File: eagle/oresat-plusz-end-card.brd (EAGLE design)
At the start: 99 x 95.3 mm, 13 parts, among them J1 J-SAMTEC-TFM-110-X1-XXX-D-RA, J2 U.FL

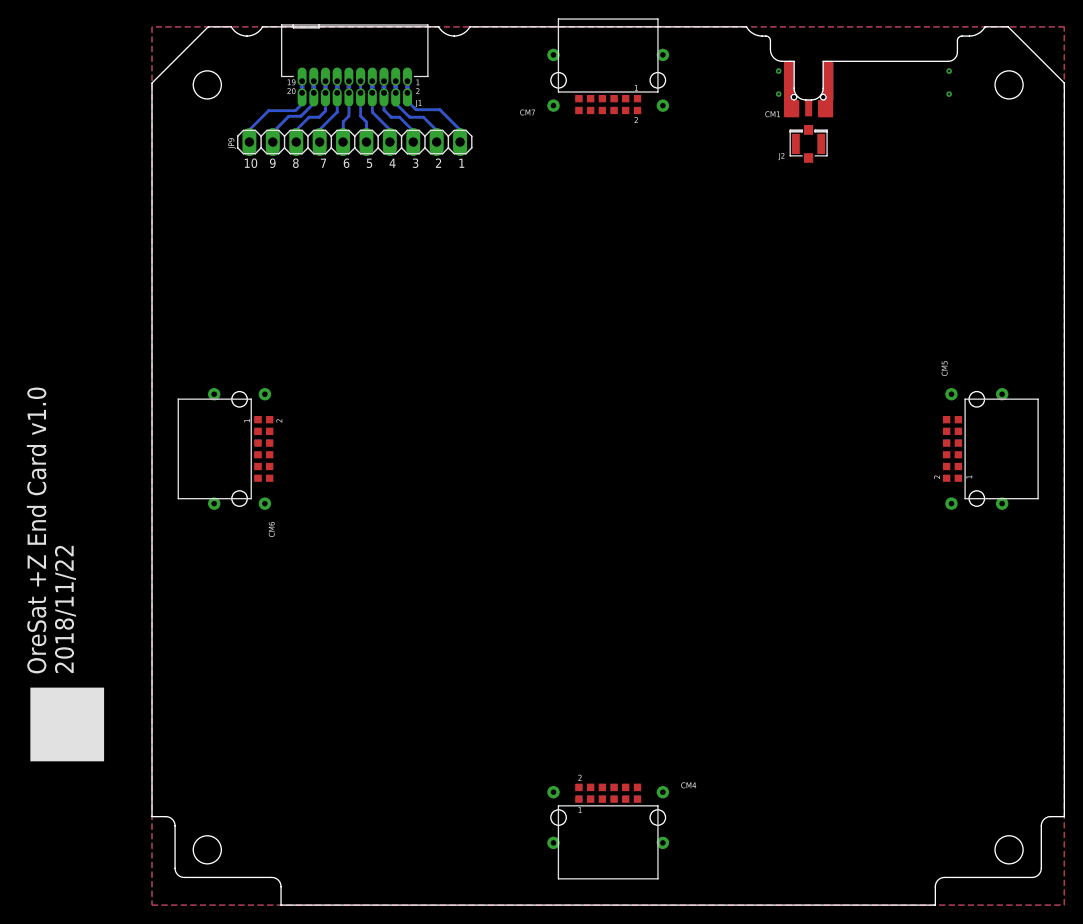
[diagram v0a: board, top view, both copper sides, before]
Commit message: Created library and placed solar connectors based on structure updates from yesterday.
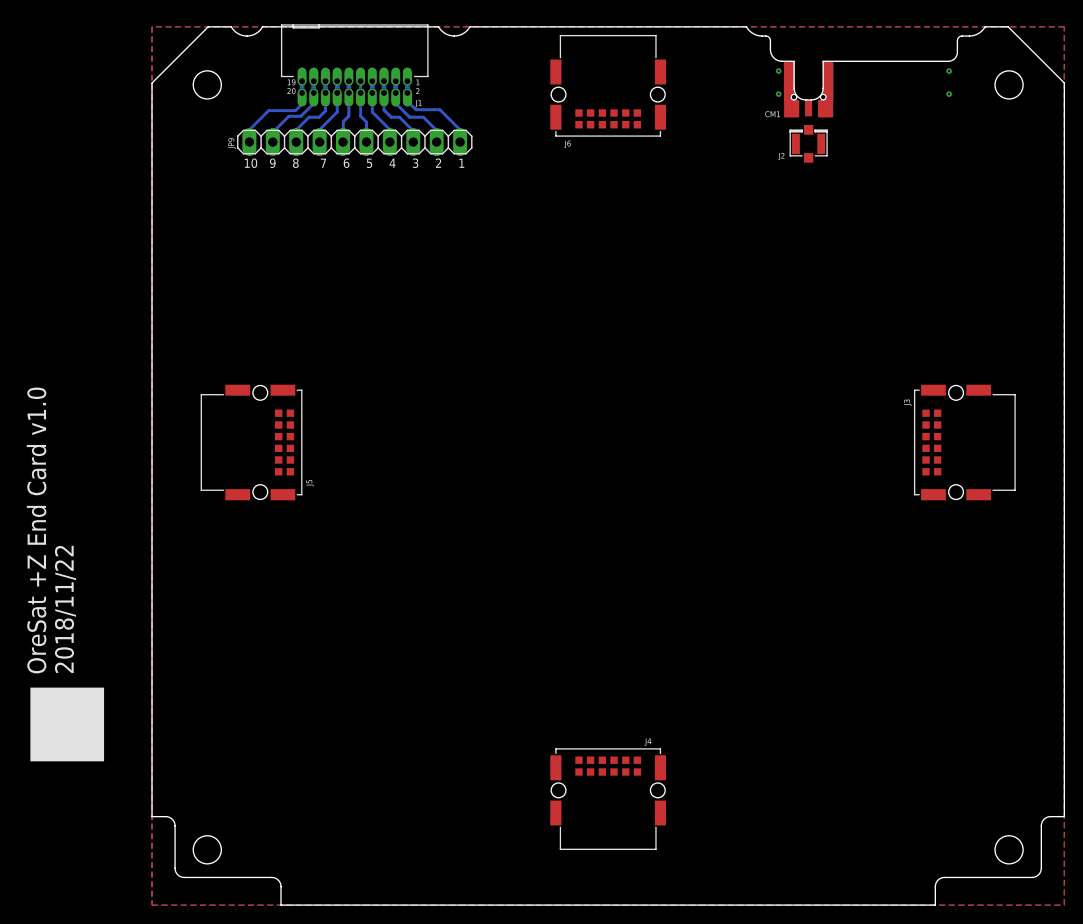
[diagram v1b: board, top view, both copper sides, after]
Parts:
- removed CM4, CM5, CM6, CM7: ORESAT-SOLARPANEL-CARD-12PIN, oresat-connectors:CON-1.27-M-RA-HARTING-1515012X401XXX
- added J3, J4, J5, J6: M55-7101242R, J-Harwin-M55-7101242:M55-7101242R
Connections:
- new net N$1: J3.1, J4.1, J5.1, J6.1
- new net N$10: J3.10, J4.10, J5.10, J6.10
- new net N$11: J3.11, J4.11, J5.11, J6.11
- new net N$12: J3.12, J4.12, J5.12, J6.12
- new net N$2: J3.2, J4.2, J5.2, J6.2
- new net N$3: J3.3, J4.3, J5.3, J6.3
- new net N$4: J3.4, J4.4, J5.4, J6.4
- new net N$5: J3.5, J4.5, J5.5, J6.5
- new net N$6: J3.6, J4.6, J5.6, J6.6
- new net N$7: J3.7, J4.7, J5.7, J6.7
- new net N$8: J3.8, J4.8, J5.8, J6.8
- new net N$9: J3.9, J4.9, J5.9, J6.9
- net GND: now also J3.P$1, J3.P$2, J3.P$3, J3.P$4, J4.P$1, J4.P$2, J4.P$3, J4.P$4, J5.P$1, J5.P$2, J5.P$3, J5.P$4, J6.P$1, J6.P$2, J6.P$3, J6.P$4

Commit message: Worked with Joe to check connectors, preliminary layout, 2 layers for now.
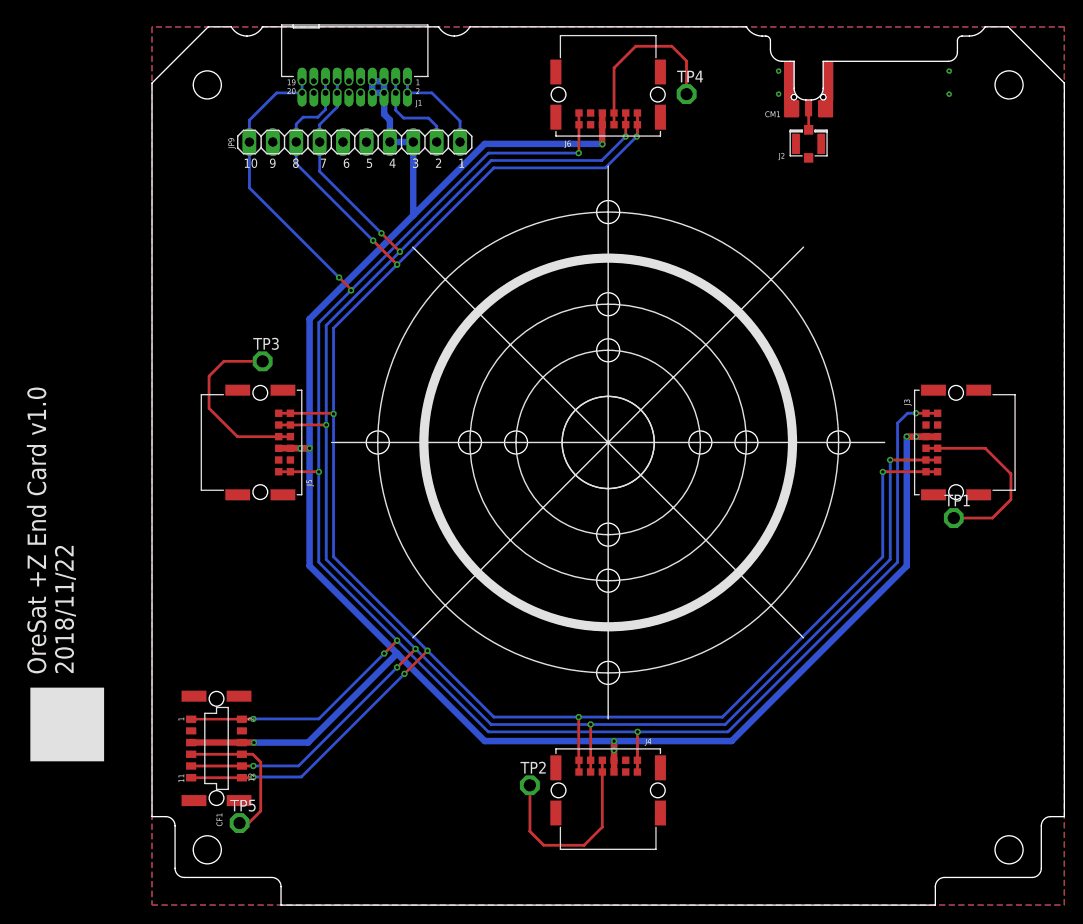
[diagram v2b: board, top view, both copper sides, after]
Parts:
- added CF1: M55-7011242R, J-Harwin-M55-6021242R:HARWIN-M55-6021242R
- added TP1, TP2, TP3, TP4, TP5: TPPAD1-13, testpad:P1-13
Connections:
- net AUX_CAN2_H renamed CAN2_H
- net AUX_CAN2_L renamed CAN2_L
- removed net AUX_!SHUTDOWN: J1.19, J1.20, JP9.10
- removed net AUX_CAN1_H: J1.13, J1.14, JP9.7
- removed net AUX_CAN1_L: J1.15, J1.16, JP9.8
- removed net AUX_GND1: J1.17, J1.18, JP9.9
- removed net AUX_GND2: J1.11, J1.12, JP9.6
- removed net AUX_GND3: J1.10, J1.9, JP9.5
- removed net AUX_VBUS1: J1.7, J1.8, JP9.4
- removed net AUX_VBUS2: J1.5, J1.6, JP9.3
- removed net N$10: J3.10, J4.10, J5.10, J6.10
- removed net N$11: J3.11, J4.11, J5.11, J6.11
- removed net N$12: J3.12, J4.12, J5.12, J6.12
- removed net N$6: J3.6, J4.6, J5.6, J6.6
- removed net N$7: J3.7, J4.7, J5.7, J6.7
- removed net N$8: J3.8, J4.8, J5.8, J6.8
- removed net N$9: J3.9, J4.9, J5.9, J6.9
- new net !SHUTDOWN: CF1.1, CF1.2, J1.19, J1.20, J3.1, J3.2, J4.1, J4.2, J5.1, J5.2, J6.1, J6.2, JP9.10
- new net CAN1_H: CF1.10, CF1.9, J1.13, J1.14, J3.10, J3.9, J4.10, J4.9, J5.10, J5.9, J6.10, J6.9, JP9.7
- new net CAN1_L: CF1.11, CF1.12, J1.15, J1.16, J3.11, J3.12, J4.11, J4.12, J5.11, J5.12, J6.11, J6.12, JP9.8
- new net VBUS: CF1.5, CF1.6, J1.5, J1.6, J1.7, J1.8, J3.5, J3.6, J4.5, J4.6, J5.5, J5.6, J6.5, J6.6, JP9.3, JP9.4
- net GND: now also CF1.3, CF1.4, CF1.P$1, CF1.P$2, CF1.P$3, CF1.P$4, J1.10, J1.11, J1.12, J1.17, J1.18, J1.9, J3.3, J3.4, J4.3, J4.4, J5.3, J5.4, J6.3, J6.4, JP9.5, JP9.6, JP9.9
- net N$1: now also J4.7, J4.8, TP2.TP; no longer J3.1, J4.1, J5.1, J6.1
- net N$2: now also J3.7, J3.8, TP1.TP; no longer J3.2, J4.2, J5.2, J6.2
- net N$3: now also CF1.7, CF1.8, TP5.TP; no longer J3.3, J4.3, J5.3, J6.3
- net N$4: now also J5.7, J5.8, TP3.TP; no longer J3.4, J4.4, J5.4, J6.4
- net N$5: now also J6.7, J6.8, TP4.TP; no longer J3.5, J4.5, J5.5, J6.5
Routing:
- net !SHUTDOWN: track 0.00 -> 230.1 mm, vias 0 -> 9
- net CAN1_L: track 0.00 -> 228.1 mm, vias 0 -> 9
- net VBUS: track 0.00 -> 224.0 mm, vias 0 -> 8
- net CAN1_H: track 0.00 -> 223.7 mm, vias 0 -> 9
- net N$1: track 0.00 -> 21.6 mm
- net N$2: track 0.00 -> 20.2 mm
- net N$4: track 0.00 -> 20.1 mm
- net N$5: track 0.00 -> 19.3 mm
- net N$3: track 0.00 -> 16.0 mm
- net AUX_!SHUTDOWN: track 10.7 -> 0.00 mm
- net AUX_GND1: track 9.21 -> 0.00 mm
- net AUX_CAN1_L: track 8.56 -> 0.00 mm
- net AUX_VBUS2: track 8.45 -> 0.00 mm
- net AUX_VBUS1: track 7.39 -> 0.00 mm
- net AUX_CAN1_H: track 7.39 -> 0.00 mm
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
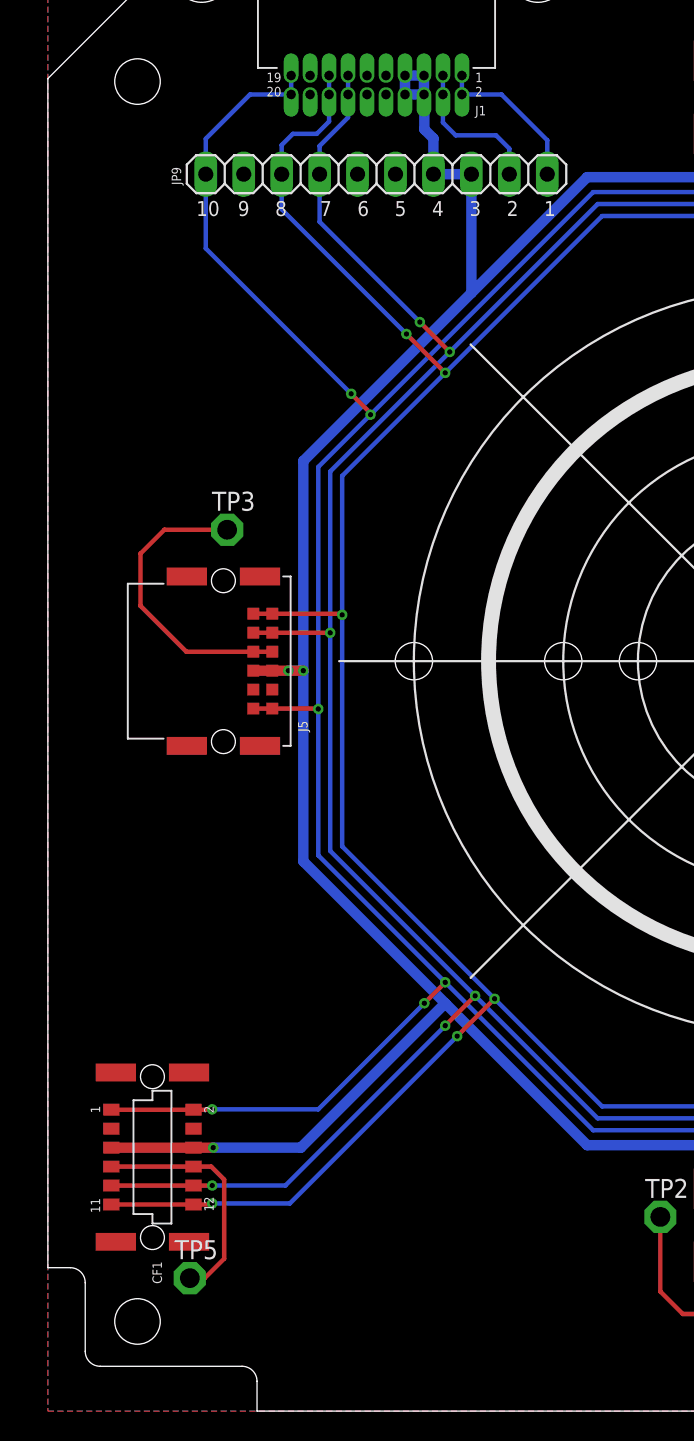
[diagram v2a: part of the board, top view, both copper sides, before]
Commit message: Updated +Z end card, with end cap attachment to magnetometers.
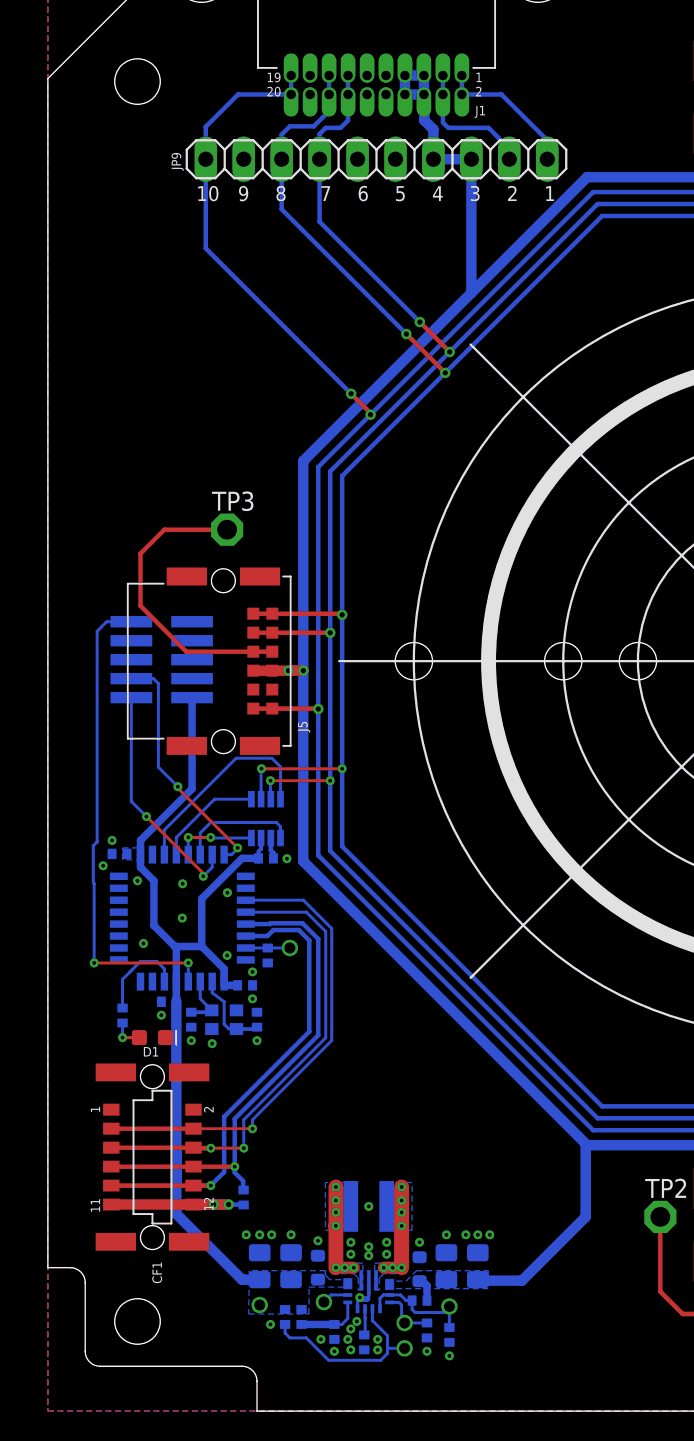
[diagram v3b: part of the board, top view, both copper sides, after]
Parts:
- removed TP5: TPPAD1-13, testpad:P1-13
- added C1: 10u, oresat-rcl:.0603-B-NOSILK
- added C10, C11: 22u, oresat-rcl:.0805-B-NOSILK
- added C12, C15, C18, C2, C8: 100n, rcl_custom:.0402-B-NOSILK
- added C13, C14: 20p, rcl_custom:.0402-B-NOSILK
- added C3, C7: 10u, oresat-rcl:.0805-B-NOSILK
- added C9: 22u, oresat-rcl:.0603-B-NOSILK
- added D1: GREEN, SparkFun-LED:LED-0603
- added J8: FTSH-105-XX-X-DV-K, J-Samtec-FTSH-105-XXX-DV-K-ARM-SWD:CON10_2X5_DUK_FTSH
- added L1: 1.5 uH, L-Coilcraft-XFL4020:L-COILCRAFT-XFL4020
- added R1, R11, R4, R8: 10k, rcl_custom:.0402-B-NOSILK
- added R10, R7: 4.7k, rcl_custom:.0402-B-NOSILK
- added R2: 470k, rcl_custom:.0402-B-NOSILK
- added R3: 150k, rcl_custom:.0402-B-NOSILK
- added R5, R6: NP, rcl_custom:.0402-B-NOSILK
- added R9: 2.7k, rcl_custom:.0402-B-NOSILK
- added TP11, TP12, TP13, TP14, TP15, TP7: TEST-POINT, Tova:2MM-TEST-POINT
- added U2: TPS63070, ic-pwr-tps63070x:TPS63070X
- added U3: TCAN330, TCAN330:SOT23-8_TI-DCN
- added U4: STM32F042K6, STM32F042K:QFP32-7X7
- added X2: 16MHZ-2.5x2mm, low-gain-radio:CRYSTAL_2.5X2
- moved JP9 1.00 mm to (22.0, 83.8)
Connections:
- removed net N$3: CF1.7, CF1.8, TP5.TP
- new net 3.3V: C10.1, C11.1, C12.2, C15.2, C18.2, C8.2, C9.1, CF1.11, CF1.12, J8.1, R10.2, R11.2, R2.2, R5.2, R7.2, TP11.1, U2.7-8, U3.3, U4.1, U4.17, U4.5
- new net BOOT1: R8.2, TP7.1, U4.31
- new net CAN_RX: U3.4, U4.21
- new net CAN_SHDN: U3.5, U4.20
- new net CAN_SILENT: U3.8, U4.19
- new net CAN_TX: U3.1, U4.22
- new net CRYSTALIN1: C14.1, U4.2, X2.1
- new net CRYSTALOUT1: C13.1, U4.3, X2.3
- new net N$7: D1.A, R9.1
- new net NRESET: J8.10, U4.4
- new net PA0: R9.2, U4.6
- new net PA1: U4.7
- new net PA15: U4.25
- new net PA2/USART2_TX: U4.8
- new net PA3/USART2_RX: U4.9
- new net PA4: U4.10
- new net PA5/SPI1_SCK: U4.11
- new net PA6/SPI1_MISO: U4.12
- new net PA7/SPI1_MOSI: U4.13
- new net PA8: U4.18
- new net PB0: U4.14
- new net PB1: U4.15
- new net PB3: U4.26
- new net PB4/I2C-!RESET: CF1.3, CF1.4, U4.27
- new net PB5/I2C-!INT: CF1.5, CF1.6, R11.1, U4.28
- new net PB6/SCL: CF1.7, CF1.8, R7.1, U4.29
- new net PB7/SDA: CF1.10, CF1.9, R10.1, U4.30
- new net SWCLK: J8.4, U4.24
- new net SWDIO: J8.2, U4.23
- new net TPS-EN2: R1.1, R6.2, TP15.1, U2.1, U2.14
- new net TPS-FB2: R2.1, R3.2, U2.5
- new net TPS-FB4: TP13.1, U2.6
- new net TPS-L1: L1.1, U2.11
- new net TPS-L2: L1.2, U2.9
- new net TPS-PG2: R5.1, TP12.1, U2.2
- new net TPS-VAUX2: C2.1, U2.3
- new net TPS-VSEL2: R4.2, TP14.1, U2.15
- net !SHUTDOWN: no longer CF1.1, CF1.2
- net CAN1_H: now also U3.7; no longer CF1.10, CF1.9
- net CAN1_L: now also U3.6; no longer CF1.11, CF1.12
- net GND: now also C1.2, C10.2, C11.2, C12.1, C13.2, C14.2, C15.1, C18.1, C2.2, C3.2, C7.2, C8.1, C9.2, CF1.1, CF1.2, D1.C, J8.3, J8.5, J8.9, R3.1, R4.1, R6.1, R8.1, U2.10, U2.4, U3.2, U4.16, U4.32, X2.2, X2.4; no longer CF1.3, CF1.4
- net VBUS: now also C1.1, C3.1, C7.1, R1.2, U2.12-13; no longer CF1.5, CF1.6
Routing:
- net 3.3V: track 0.00 -> 74.8 mm, vias 0 -> 2
- net PB6/SCL: track 0.00 -> 32.9 mm, vias 0 -> 1
- net PB5/I2C-!INT: track 0.00 -> 32.8 mm, vias 0 -> 2
- net NRESET: track 0.00 -> 32.4 mm, vias 0 -> 2
- net PB7/SDA: track 0.00 -> 31.8 mm, vias 0 -> 1
- net PB4/I2C-!RESET: track 0.00 -> 31.6 mm, vias 0 -> 1
- net !SHUTDOWN: track 230.1 -> 204.6 mm, vias 9 -> 6
- net CAN1_L: track 228.1 -> 204.2 mm, vias 9 -> 8
- net CAN1_H: track 223.7 -> 200.0 mm, vias 9 -> 8
- net SWCLK: track 0.00 -> 16.4 mm, vias 0 -> 2
- net N$3: track 16.0 -> 0.00 mm
- net SWDIO: track 0.00 -> 15.7 mm, vias 0 -> 2
- net CAN_SILENT: track 0.00 -> 13.8 mm
- net TPS-PG2: track 0.00 -> 12.9 mm
- net VBUS: track 224.0 -> 213.2 mm, vias 8 -> 7
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- added copper zone on layer 16, net 3.3V
- added copper zone on layer 16, net TPS-L1
- added copper zone on layer 16, net TPS-L2
- added copper zone on layer 16, net VBUS
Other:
- board text added: "3.3V"
- board text added: "Vin"

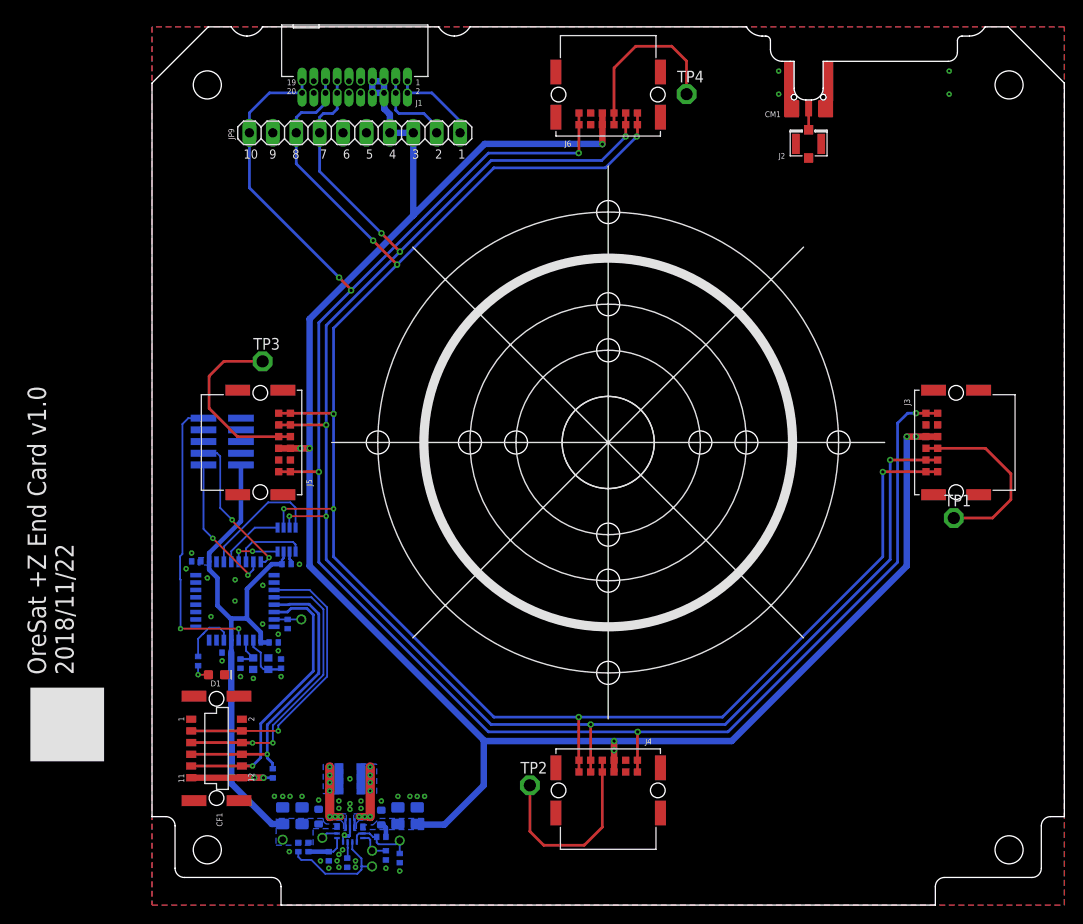
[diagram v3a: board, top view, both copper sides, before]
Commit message: +Z end cards ready for mfg, as far as we know!
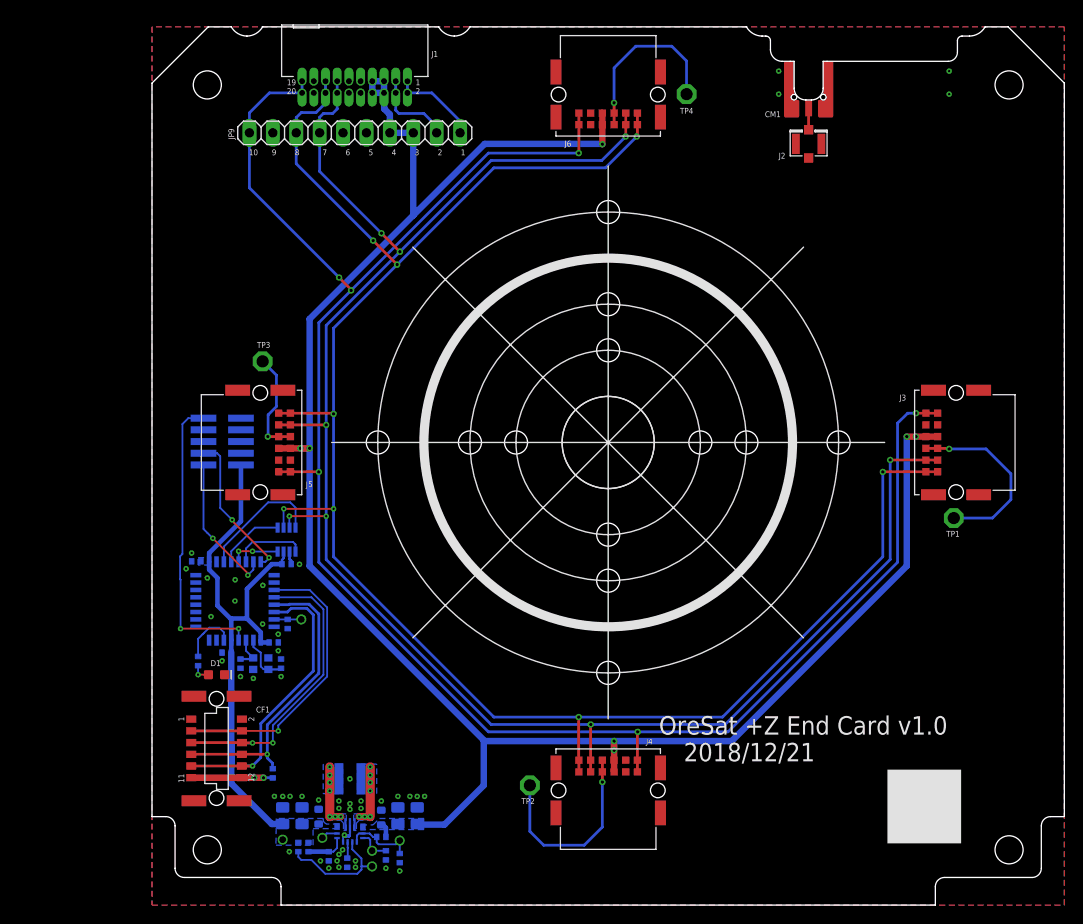
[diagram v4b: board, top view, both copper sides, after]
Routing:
- net N$4: track 20.1 -> 11.6 mm, vias 0 -> 1
- net N$1: vias 0 -> 1
- net N$5: vias 0 -> 1
- net N$2: vias 0 -> 1
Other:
- board text added: "2018/12/21"
- board text removed: "2018/11/22"
